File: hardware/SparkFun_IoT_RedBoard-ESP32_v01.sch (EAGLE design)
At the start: 113 parts, among them J1 5.5x2.1mm Barrel, J13 QWIIC_RIGHT_ANGLE, J15 MICRO-SD-PUSH-PUSH-EXT-PIN, J2 USB C, J3 USB_SOLDER_PADS, J5 M10NO_SILK, Q1 MBT3904DW1T1, Q11 20V/4.2A/52mΩ/1.4W, Q13 20V/4.2A/52mΩ/1.4W, Q3 20V/4.2A/52mΩ/1.4W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

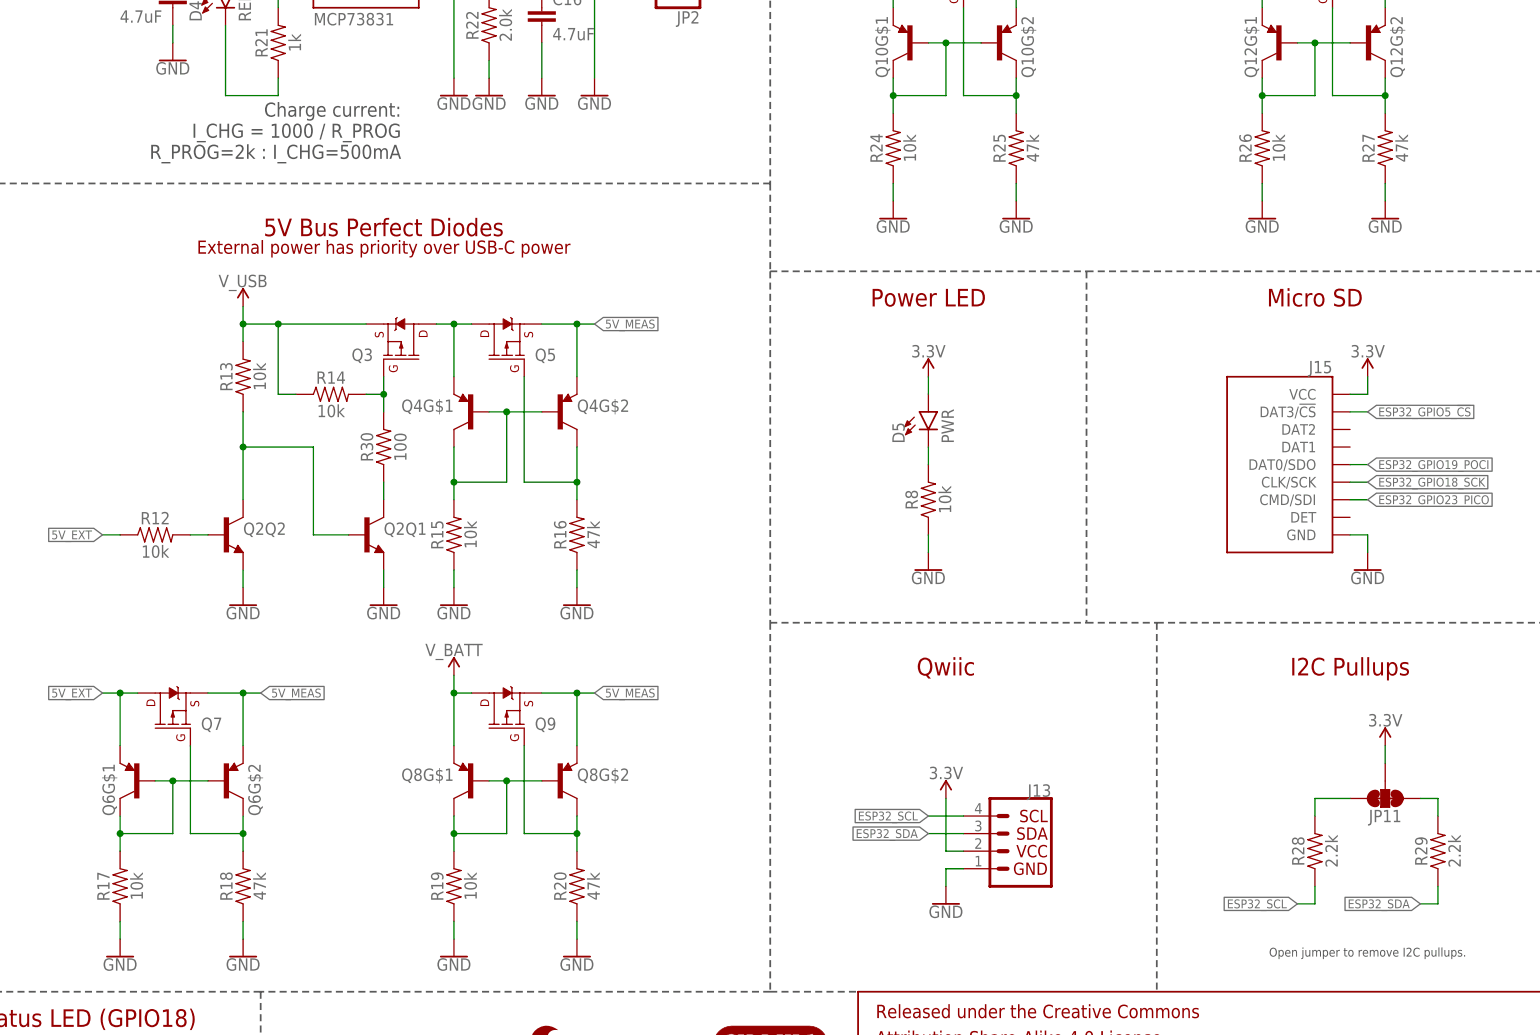
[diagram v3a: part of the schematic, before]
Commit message: Increase resistors on perfect diodes to reduce quiescent current
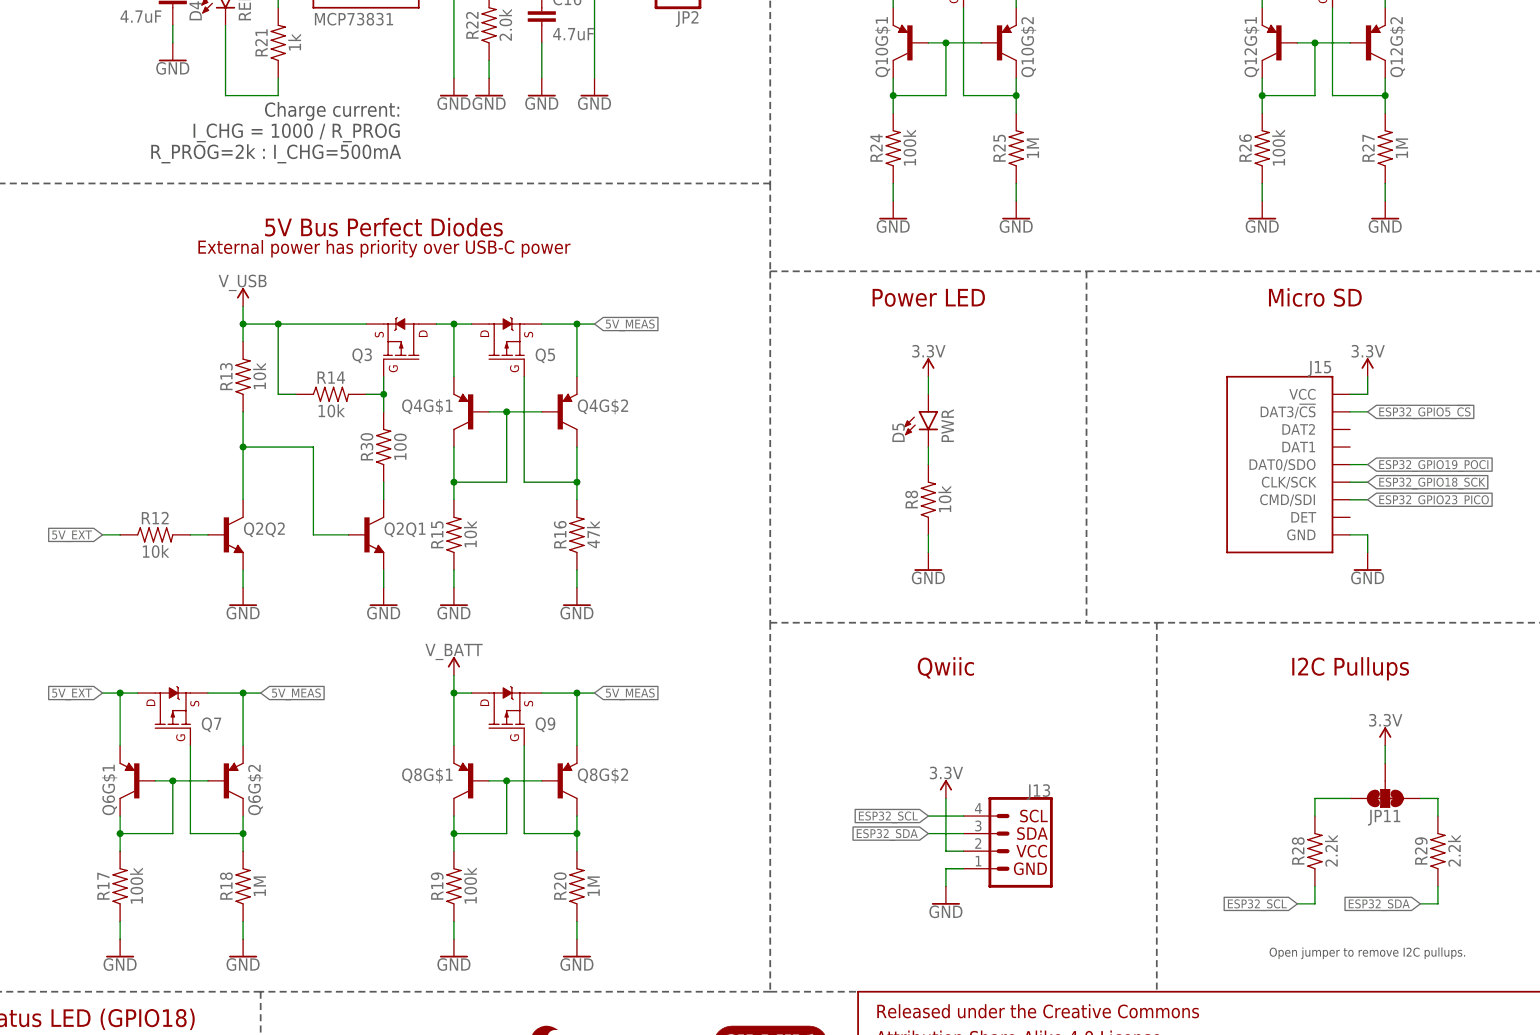
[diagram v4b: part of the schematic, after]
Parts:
- R17, R19, R24, R26: value 10k -> 100k; device SparkFun-Resistors:10KOHM-0603-1/10W-1% -> SparkFun-Resistors:100KOHM-0603-1/10W-1%
- R18, R20, R25, R27: value 47k -> 1M; device SparkFun-Resistors:47KOHM-0603-1/10W-1% -> SparkFun-Resistors:1MOHM-0603-1/4W-5%
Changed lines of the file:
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@@
 <drawing>
 <settings>
-<setting alwaysvectorfont="no"/>
+<setting alwaysvectorfont="yes"/>
 <setting keepoldvectorfont="yes"/>
 <setting verticaltext="up"/>
@@
 <part name="Q6" library="SparkFun-DiscreteSemi" deviceset="TRANS_PNP_DUAL" device="SOT-363" package3d_urn="urn:adsk.eagle:package:29757/2"/>
 <part name="Q7" library="SparkFun-DiscreteSemi" deviceset="MOSFET_PCH" device="-DMG2305UX-7" value="20V/4.2A/52mΩ/1.4W"/>
-<part name="R17" library="SparkFun-Resistors" deviceset="10KOHM" device="-0603-1/10W-1%" value="10k"/>
-<part name="R18" library="SparkFun-Resistors" deviceset="47KOHM" device="-0603-1/10W-1%" value="47k"/>
+<part name="R17" library="SparkFun-Resistors" deviceset="100KOHM" device="-0603-1/10W-1%" value="100k"/>
+<part name="R18" library="SparkFun-Resistors" deviceset="1MOHM" device="-0603-1/4W-5%" value="1M"/>
 <part name="GND27" library="SparkFun-PowerSymbols" deviceset="GND" device=""/>
 <part name="GND28" library="SparkFun-PowerSymbols" deviceset="GND" device=""/>
 <part name="Q8" library="SparkFun-DiscreteSemi" deviceset="TRANS_PNP_DUAL" device="SOT-363" package3d_urn="urn:adsk.eagle:package:29757/2"/>
 <part name="Q9" library="SparkFun-DiscreteSemi" deviceset="MOSFET_PCH" device="-DMG2305UX-7" value="20V/4.2A/52mΩ/1.4W"/>
-<part name="R19" library="SparkFun-Resistors" deviceset="10KOHM" device="-0603-1/10W-1%" value="10k"/>
-<part name="R20" library="SparkFun-Resistors" deviceset="47KOHM" device="-0603-1/10W-1%" value="47k"/>
+<part name="R19" library="SparkFun-Resistors" deviceset="100KOHM" device="-0603-1/10W-1%" value="100k"/>
+<part name="R20" library="SparkFun-Resistors" deviceset="1MOHM" device="-0603-1/4W-5%" value="1M"/>
 <part name="GND39" library="SparkFun-PowerSymbols" deviceset="GND" device=""/>
 <part name="GND40" library="SparkFun-PowerSymbols" deviceset="GND" device=""/>
@@
 <part name="Q10" library="SparkFun-DiscreteSemi" deviceset="TRANS_PNP_DUAL" device="SOT-363" package3d_urn="urn:adsk.eagle:package:29757/2"/>
 <part name="Q11" library="SparkFun-DiscreteSemi" deviceset="MOSFET_PCH" device="-DMG2305UX-7" value="20V/4.2A/52mΩ/1.4W"/>
-<part name="R24" library="SparkFun-Resistors" deviceset="10KOHM" device="-0603-1/10W-1%" value="10k"/>
-<part name="R25" library="SparkFun-Resistors" deviceset="47KOHM" device="-0603-1/10W-1%" value="47k"/>
+<part name="R24" library="SparkFun-Resistors" deviceset="100KOHM" device="-0603-1/10W-1%" value="100k"/>
+<part name="R25" library="SparkFun-Resistors" deviceset="1MOHM" device="-0603-1/4W-5%" value="1M"/>
 <part name="GND38" library="SparkFun-PowerSymbols" deviceset="GND" device=""/>
 <part name="GND41" library="SparkFun-PowerSymbols" deviceset="GND" device=""/>
@@
 <part name="Q12" library="SparkFun-DiscreteSemi" deviceset="TRANS_PNP_DUAL" device="SOT-363" package3d_urn="urn:adsk.eagle:package:29757/2"/>
 <part name="Q13" library="SparkFun-DiscreteSemi" deviceset="MOSFET_PCH" device="-DMG2305UX-7" value="20V/4.2A/52mΩ/1.4W"/>
-<part name="R26" library="SparkFun-Resistors" deviceset="10KOHM" device="-0603-1/10W-1%" value="10k"/>
-<part name="R27" library="SparkFun-Resistors" deviceset="47KOHM" device="-0603-1/10W-1%" value="47k"/>
+<part name="R26" library="SparkFun-Resistors" deviceset="100KOHM" device="-0603-1/10W-1%" value="100k"/>
+<part name="R27" library="SparkFun-Resistors" deviceset="1MOHM" device="-0603-1/4W-5%" value="1M"/>
 <part name="GND44" library="SparkFun-PowerSymbols" deviceset="GND" device=""/>
 <part name="GND52" library="SparkFun-PowerSymbols" deviceset="GND" device=""/>

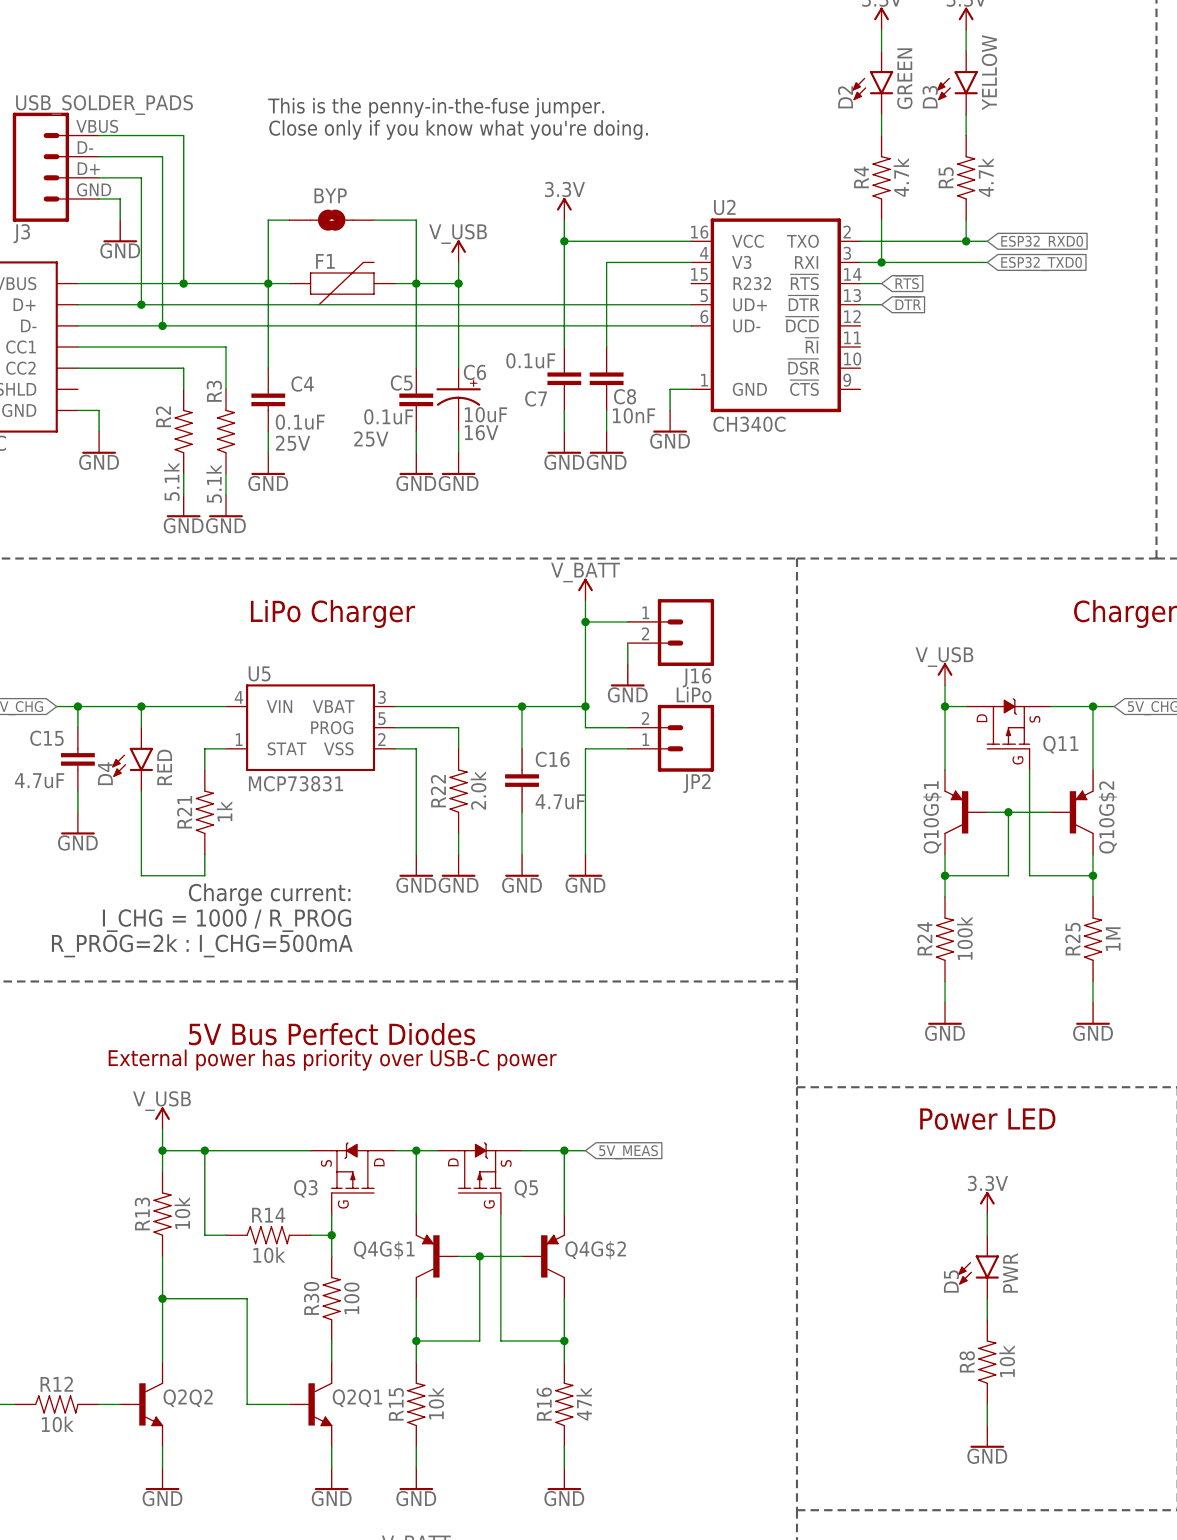
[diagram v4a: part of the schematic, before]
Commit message: Update cosmetic components and silk
Change power LED to red
Change charge LED to yellow
Change green/yellow LED resistors to 1k
Change red LED resistor to 2.2k
Update some top pin silk labels to include pin numbers
Fix RX silk to be "RX-0" instead of "RX-1"
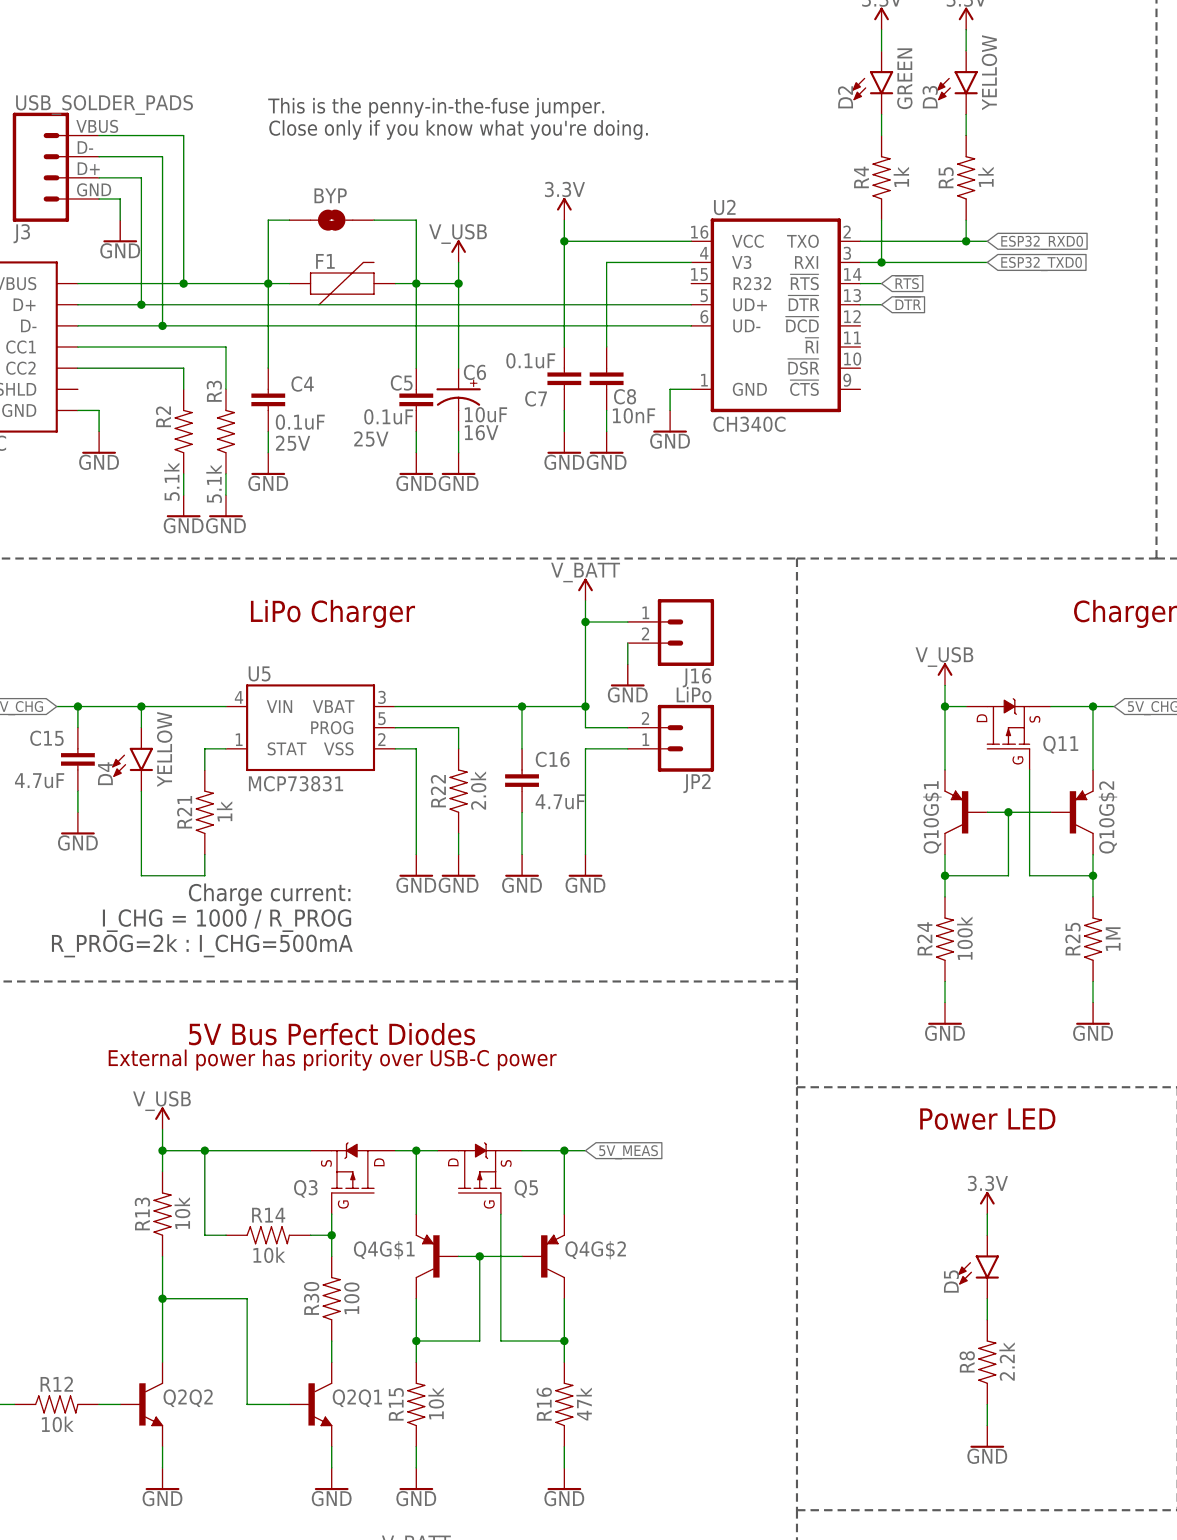
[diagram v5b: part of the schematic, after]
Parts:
- D4: value RED -> YELLOW; device SparkFun-LED:LED-RED_HIDDENSILK -> SparkFun-LED:LED-YELLOW_HIDDENSILK
- D5: value PWR -> GREEN; device SparkFun-LED:LED-GREEN_HIDDENSILK -> SparkFun-LED:LED-RED_HIDDENSILK
- R4, R5: value 4.7k -> 1k; device SparkFun-Resistors:4.7KOHM-0603-1/10W-1% -> SparkFun-Resistors:1KOHM-0603-1/10W-1%
- R8: value 10k -> 2.2k; device SparkFun-Resistors:10KOHM-0603-1/10W-1% -> SparkFun-Resistors:2.2KOHM-0603-1/10W-1%
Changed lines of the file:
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@@
 <drawing>
 <settings>
-<setting alwaysvectorfont="yes"/>
+<setting alwaysvectorfont="no"/>
 <setting keepoldvectorfont="yes"/>
 <setting verticaltext="up"/>
@@
 </part>
 <part name="C8" library="SparkFun-Capacitors" deviceset="10NF" device="-0603-50V-10%" value="10nF"/>
-<part name="R5" library="SparkFun-Resistors" deviceset="4.7KOHM" device="-0603-1/10W-1%" value="4.7k"/>
+<part name="R5" library="SparkFun-Resistors" deviceset="1KOHM" device="-0603-1/10W-1%" value="1k"/>
 <part name="C7" library="SparkFun-Capacitors" deviceset="0.1UF" device="-0603-25V-(+80/-20%)" value="0.1uF"/>
-<part name="R4" library="SparkFun-Resistors" deviceset="4.7KOHM" device="-0603-1/10W-1%" value="4.7k"/>
+<part name="R4" library="SparkFun-Resistors" deviceset="1KOHM" device="-0603-1/10W-1%" value="1k"/>
 <part name="J2" library="SparkFun-Connectors" deviceset="USB_C" device="_2-LAYER_PADS" value="USB C"/>
 <part name="U2" library="SparkFun-IC-Comms" deviceset="CH340C" device=""/>
@@
 <part name="R22" library="SparkFun-Resistors" deviceset="2.0KOHM" device="-0603-1/10W-5%" value="2.0k"/>
 <part name="C15" library="SparkFun-Capacitors" deviceset="4.7UF" device="-0603-35V-(20%)" value="4.7uF"/>
-<part name="D4" library="SparkFun-LED" deviceset="LED-RED" device="_HIDDENSILK" value="RED"/>
+<part name="D4" library="SparkFun-LED" deviceset="LED-YELLOW" device="_HIDDENSILK" value="YELLOW"/>
 <part name="SUPPLY4" library="SparkFun-PowerSymbols" deviceset="V_BATT" device=""/>
 <part name="GND4" library="SparkFun-PowerSymbols" deviceset="GND" device=""/>
@@
 <part name="J14" library="SparkFun-Connectors" deviceset="CONN_02" device="1X02_NO_SILK"/>
 <part name="SUPPLY17" library="SparkFun-PowerSymbols" deviceset="5V" device=""/>
-<part name="R8" library="SparkFun-Resistors" deviceset="10KOHM" device="-0603-1/10W-1%" value="10k"/>
+<part name="R8" library="SparkFun-Resistors" deviceset="2.2KOHM" device="-0603-1/10W-1%" value="2.2k"/>
 <part name="SUPPLY6" library="SparkFun-PowerSymbols" deviceset="3.3V" device=""/>
-<part name="D5" library="SparkFun-LED" deviceset="LED-GREEN" device="_HIDDENSILK" value="PWR"/>
+<part name="D5" library="SparkFun-LED" deviceset="LED-RED" device="_HIDDENSILK" value="GREEN"/>
 <part name="GND51" library="SparkFun-PowerSymbols" deviceset="GND" device=""/>
 <part name="LOGO1" library="SparkFun-Aesthetics" deviceset="SFE_LOGO_NAME" device=".1_INCH" value="SFE_LOGO_NAME.1_INCH"/>
@@
 <instance part="D5" gate="G$1" x="340.36" y="119.38" smashed="yes">
 <attribute name="NAME" x="336.931" y="114.808" size="1.778" layer="95" font="vector" rot="R90"/>
-<attribute name="VALUE" x="342.265" y="114.808" size="1.778" layer="96" font="vector" rot="R90" align="top-left"/>
 </instance>
 <instance part="GND51" gate="1" x="340.36" y="96.52" smashed="yes">
